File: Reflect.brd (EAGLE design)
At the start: 36.6 x 9.1 mm, 8 parts

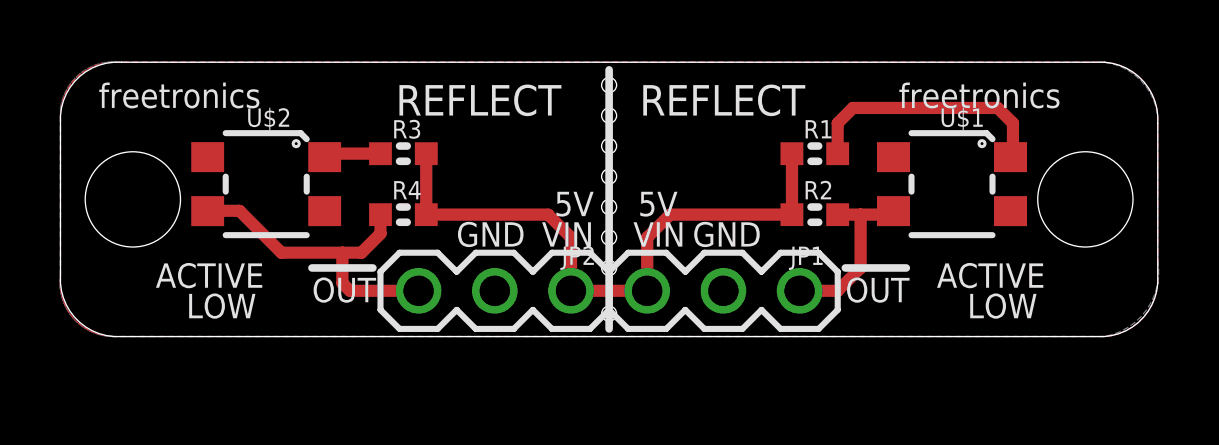
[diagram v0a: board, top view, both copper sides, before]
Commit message: Split ground pour into two halves to fix unrouted ground airwire. Added schematic note that although only one VCC pin needs to be connected both ground pins need to be connected if both sensors are used on an unsplit board.
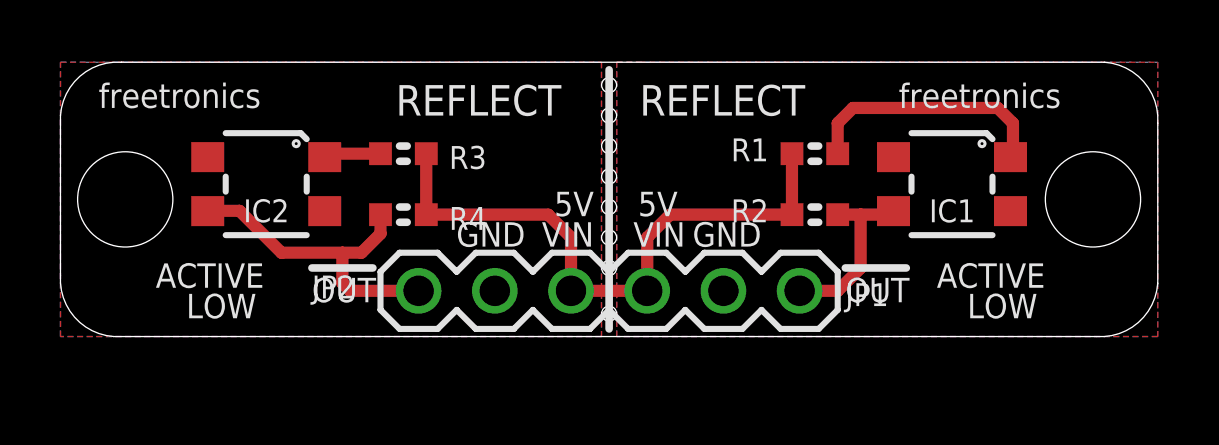
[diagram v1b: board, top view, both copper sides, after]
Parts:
- renumbered U$1 to IC1, U$2 to IC2
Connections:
- removed net GND: IC1.2, IC1.4, IC2.2, IC2.4, JP1.2, JP2.2
- new net GND1: IC2.2, IC2.4, JP2.2
- new net GND2: IC1.2, IC1.4, JP1.2
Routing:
- added copper zone on layer 1, net GND1
- added copper zone on layer 16, net GND1
- added copper zone on layer 1, net GND2
- added copper zone on layer 16, net GND2
- removed copper zone on layer 1, net GND
- removed copper zone on layer 16, net GND

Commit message: New version with GNDs connected.
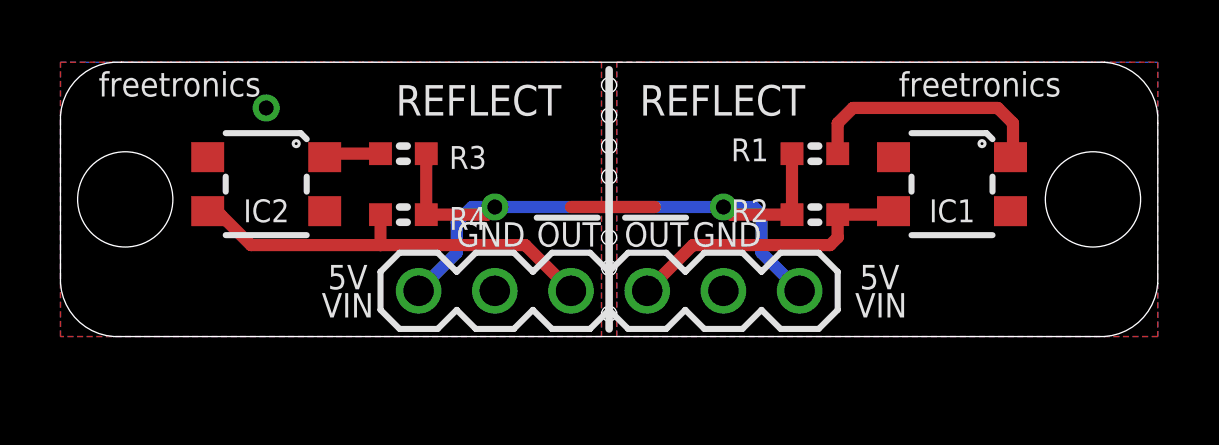
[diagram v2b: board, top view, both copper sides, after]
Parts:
- moved JP1 5.08 mm to (19.6, 1.52), flipped to the bottom
- moved JP2 5.08 mm to (11.9, 1.52), flipped to the bottom
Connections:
- removed net GND1: IC2.2, IC2.4, JP2.2
- removed net GND2: IC1.2, IC1.4, JP1.2
- new net GND: IC1.2, IC1.4, IC2.2, IC2.4, JP1.2, JP2.2
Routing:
- net VCC: track 20.4 -> 25.2 mm, vias 0 -> 2
- net OUT2: track 6.03 -> 9.76 mm
- net OUT1: track 10.9 -> 14.2 mm
- net GND: track 0.00 -> 2.79 mm, vias 0 -> 1
- added copper zone on layer 1, net GND
- added copper zone on layer 16, net GND
- removed copper zone on layer 1, net GND1
- removed copper zone on layer 16, net GND1
- removed copper zone on layer 1, net GND2
- removed copper zone on layer 16, net GND2
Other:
- board text added: "(5V)"
- board text removed: "ACTIVE"
- board text removed: "LOW"

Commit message: Tweaks to schematic and PCB for v1.0 release
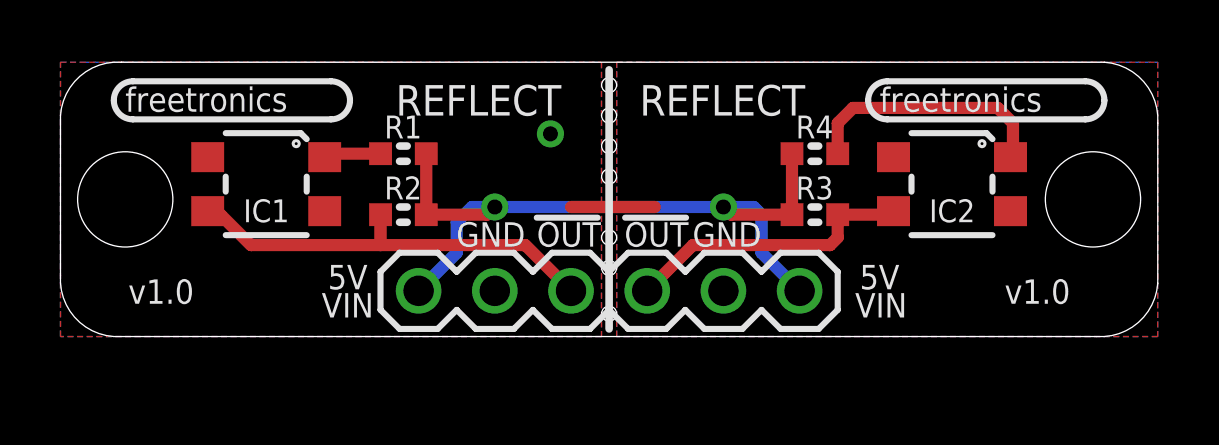
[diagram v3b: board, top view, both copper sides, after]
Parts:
- R1: value 100 -> 100R
- R3: value 100 -> 10k
- R4: value 10k -> 100R
- moved IC1 22.9 mm to (6.86, 5.08)
- moved IC2 22.9 mm to (29.7, 5.08)
- moved R3 13.9 mm to (25.1, 4.06)
- moved R4 13.9 mm to (25.1, 6.10)
- moved R1 13.7 mm to (11.4, 6.10)
- moved R2 13.7 mm to (11.4, 4.06)
- moved JP1 7.62 mm to (11.9, 1.52)
- moved JP2 7.62 mm to (19.6, 1.52)
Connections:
- net N$1: now also IC1.1, R1.1; no longer IC2.1, R3.1
- net N$3: now also IC2.1, R4.2; no longer IC1.1, R1.2
- net OUT1: now also IC1.3, JP1.3, R2.1; no longer IC2.3, JP2.3, R4.1
- net OUT2: now also IC2.3, JP2.1, R3.2; no longer IC1.3, JP1.1, R2.2
- net VCC: now also JP1.1, JP2.3, R1.2, R2.2, R3.1, R4.1; no longer JP1.3, JP2.1, R1.1, R2.1, R3.2, R4.2
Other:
- board text added: "v1.0"
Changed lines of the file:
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@@
 <?xml version="1.0" encoding="utf-8"?>
 <!DOCTYPE eagle SYSTEM "eagle.dtd">
-<eagle version="6.5.0">
+<eagle version="6.3">
 <drawing>
 <settings>
@@
 <setting verticaltext="up"/>
 </settings>
-<grid distance="0.005" unitdist="inch" unit="inch" style="dots" multiple="1" display="yes" altdistance="0.005" altunitdist="inch" altunit="inch"/>
+<grid distance="0.005" unitdist="inch" unit="inch" style="dots" multiple="1" display="no" altdistance="0.005" altunitdist="inch" altunit="inch"/>
 <layers>
 <layer number="1" name="Top" color="4" fill="1" visible="yes" active="yes"/>
@@
 <text x="11.176" y="7.366" size="1.016" layer="21" ratio="15">REFLECT</text>
 <text x="19.304" y="7.366" size="1.016" layer="21" ratio="15">REFLECT</text>
-<text x="27.94" y="8.001" size="0.8128" layer="21" ratio="15">freetronics</text>
-<text x="1.27" y="8.001" size="0.8128" layer="21" ratio="15">freetronics</text>
+<text x="2.159" y="7.493" size="0.8128" layer="21" ratio="15">freetronics</text>
 <text x="12.954" y="3.048" size="0.8128" layer="22" font="vector" ratio="15" rot="MR0">VIN</text>
 <text x="23.114" y="3.048" size="0.8128" layer="22" font="vector" ratio="15" rot="MR0">GND</text>
@@
 <wire x1="23.368" y1="2.159" x2="24.003" y2="2.794" width="0.2032" layer="21"/>
 <text x="28.2194" y="1.4478" size="0.8128" layer="21" font="vector" ratio="15" rot="R180">VIN</text>
+<text x="2.2606" y="1.0922" size="0.8128" layer="21" font="vector" ratio="15">v1.0</text>
+<text x="31.4706" y="1.0922" size="0.8128" layer="21" font="vector" ratio="15">v1.0</text>
+<wire x1="2.413" y1="8.509" x2="1.778" y2="7.874" width="0.2032" layer="21" curve="90"/>
+<wire x1="1.778" y1="7.874" x2="2.413" y2="7.239" width="0.2032" layer="21" curve="90"/>
+<wire x1="2.413" y1="7.239" x2="9.017" y2="7.239" width="0.2032" layer="21"/>
+<wire x1="9.017" y1="7.239" x2="9.652" y2="7.874" width="0.2032" layer="21" curve="90"/>
+<wire x1="9.652" y1="7.874" x2="9.017" y2="8.509" width="0.2032" layer="21" curve="90"/>
+<wire x1="9.017" y1="8.509" x2="2.413" y2="8.509" width="0.2032" layer="21"/>
+<text x="27.305" y="7.493" size="0.8128" layer="21" ratio="15">freetronics</text>
+<wire x1="27.559" y1="8.509" x2="26.924" y2="7.874" width="0.2032" layer="21" curve="90"/>
+<wire x1="26.924" y1="7.874" x2="27.559" y2="7.239" width="0.2032" layer="21" curve="90"/>
+<wire x1="27.559" y1="7.239" x2="34.163" y2="7.239" width="0.2032" layer="21"/>
+<wire x1="34.163" y1="7.239" x2="34.798" y2="7.874" width="0.2032" layer="21" curve="90"/>
+<wire x1="34.798" y1="7.874" x2="34.163" y2="8.509" width="0.2032" layer="21" curve="90"/>
+<wire x1="34.163" y1="8.509" x2="27.559" y2="8.509" width="0.2032" layer="21"/>
+<circle x="7.874" y="6.477" radius="0.127" width="0.2032" layer="51"/>
+<circle x="30.734" y="6.477" radius="0.127" width="0.2032" layer="51"/>
 </plain>
 <attributes>
@@
 </autorouter>
 <elements>
-<element name="IC1" library="freetronics-original" package="QRE1113GR" value="QRE1113GR" x="29.718" y="5.08" smashed="yes" rot="R180">
+<element name="IC2" library="freetronics-original" package="QRE1113GR" value="QRE1113GR" x="29.718" y="5.08" smashed="yes" rot="R180">
 <attribute name="NAME" x="28.956" y="3.81" size="0.762" layer="25" ratio="15"/>
 <attribute name="VALUE" x="26.416" y="7.112" size="0.762" layer="27" ratio="15"/>
 </element>
-<element name="R1" library="freetronics-original" package="0603" value="100" x="25.146" y="6.096" smashed="yes">
-<attribute name="NAME" x="22.352" y="5.842" size="0.762" layer="25" font="vector" ratio="15"/>
+<element name="R4" library="freetronics-original" package="0603" value="100R" x="25.146" y="6.096" smashed="yes">
+<attribute name="NAME" x="24.511" y="6.604" size="0.762" layer="25" font="vector" ratio="15"/>
 <attribute name="VALUE" x="24.384" y="5.588" size="0.762" layer="27" font="vector" ratio="15"/>
 </element>
-<element name="R2" library="freetronics-original" package="0603" value="10k" x="25.146" y="4.064" smashed="yes">
-<attribute name="NAME" x="22.352" y="3.81" size="0.762" layer="25" font="vector" ratio="15"/>
+<element name="R3" library="freetronics-original" package="0603" value="10k" x="25.146" y="4.064" smashed="yes">
+<attribute name="NAME" x="24.511" y="4.572" size="0.762" layer="25" font="vector" ratio="15"/>
 <attribute name="VALUE" x="24.384" y="3.81" size="0.762" layer="27" font="vector" ratio="15"/>
 </element>
-<element name="JP1" library="freetronics-original" package="1X03" value="" x="19.558" y="1.524" smashed="yes" rot="MR180">
+<element name="JP2" library="freetronics-original" package="1X03" value="" x="19.558" y="1.524" smashed="yes" rot="MR180">
 <attribute name="NAME" x="18.034" y="1.016" size="0.762" layer="26" ratio="15" rot="MR0"/>
 <attribute name="VALUE" x="18.288" y="4.699" size="1.27" layer="28" rot="MR180"/>
 </element>
-<element name="IC2" library="freetronics-original" package="QRE1113GR" value="QRE1113GR" x="6.858" y="5.08" smashed="yes" rot="R180">
+<element name="IC1" library="freetronics-original" package="QRE1113GR" value="QRE1113GR" x="6.858" y="5.08" smashed="yes" rot="R180">
 <attribute name="NAME" x="6.096" y="3.81" size="0.762" layer="25" ratio="15"/>
 <attribute name="VALUE" x="3.81" y="7.112" size="0.762" layer="27" ratio="15"/>
 </element>
-<element name="R3" library="freetronics-original" package="0603" value="100" x="11.43" y="6.096" smashed="yes">
-<attribute name="NAME" x="12.954" y="5.588" size="0.762" layer="25" font="vector" ratio="15"/>
+<element name="R1" library="freetronics-original" package="0603" value="100R" x="11.43" y="6.096" smashed="yes">
+<attribute name="NAME" x="10.795" y="6.604" size="0.762" layer="25" font="vector" ratio="15"/>
 <attribute name="VALUE" x="10.668" y="5.842" size="0.762" layer="27" font="vector" ratio="15"/>
 </element>
-<element name="R4" library="freetronics-original" package="0603" value="10k" x="11.43" y="4.064" smashed="yes">
-<attribute name="NAME" x="12.954" y="3.556" size="0.762" layer="25" font="vector" ratio="15"/>
+<element name="R2" library="freetronics-original" package="0603" value="10k" x="11.43" y="4.064" smashed="yes">
+<attribute name="NAME" x="10.795" y="4.572" size="0.762" layer="25" font="vector" ratio="15"/>
 <attribute name="VALUE" x="10.668" y="3.81" size="0.762" layer="27" font="vector" ratio="15"/>
 </element>
-<element name="JP2" library="freetronics-original" package="1X03" value="" x="11.938" y="1.524" smashed="yes" rot="MR180">
+<element name="JP1" library="freetronics-original" package="1X03" value="" x="11.938" y="1.524" smashed="yes" rot="MR180">
 <attribute name="NAME" x="20.574" y="1.27" size="0.762" layer="26" ratio="15" rot="MR0"/>
 <attribute name="VALUE" x="10.668" y="4.699" size="1.27" layer="28" rot="MR180"/>
@@
 <signals>
 <signal name="OUT2">
-<contactref element="JP1" pad="1"/>
-<contactref element="R2" pad="2"/>
-<contactref element="IC1" pad="3"/>
+<contactref element="JP2" pad="1"/>
+<contactref element="R3" pad="2"/>
+<contactref element="IC2" pad="3"/>
 <wire x1="25.908" y1="4.064" x2="27.652" y2="4.064" width="0.4064" layer="1"/>
 <wire x1="27.652" y1="4.064" x2="27.768" y2="4.18" width="0.4064" layer="1"/>
@@
 </signal>
 <signal name="VCC">
-<contactref element="JP1" pad="3"/>
-<contactref element="JP2" pad="1"/>
-<contactref element="R4" pad="2"/>
-<contactref element="R3" pad="2"/>
+<contactref element="JP2" pad="3"/>
+<contactref element="JP1" pad="1"/>
+<contactref element="R2" pad="2"/>
+<contactref element="R1" pad="2"/>
 <wire x1="12.192" y1="4.064" x2="12.192" y2="6.096" width="0.4064" layer="1"/>
-<contactref element="R1" pad="1"/>
-<contactref element="R2" pad="1"/>
+<contactref element="R4" pad="1"/>
+<contactref element="R3" pad="1"/>
 <wire x1="24.384" y1="4.064" x2="24.384" y2="6.096" width="0.4064" layer="1"/>
 <wire x1="12.192" y1="4.064" x2="14.224" y2="4.064" width="0.4064" layer="1"/>
@@
 </signal>
 <signal name="N$1">
-<contactref element="R3" pad="1"/>
-<contactref element="IC2" pad="1"/>
+<contactref element="R1" pad="1"/>
+<contactref element="IC1" pad="1"/>
 <wire x1="8.819" y1="5.969" x2="8.808" y2="5.98" width="0.4064" layer="1"/>
 <wire x1="10.668" y1="6.096" x2="8.924" y2="6.096" width="0.4064" layer="1"/>
@@
 </signal>
 <signal name="OUT1">
-<contactref element="JP2" pad="3"/>
-<contactref element="R4" pad="1"/>
-<contactref element="IC2" pad="3"/>
+<contactref element="JP1" pad="3"/>
+<contactref element="R2" pad="1"/>
+<contactref element="IC1" pad="3"/>
 <wire x1="5.08" y1="4.064" x2="5.334" y2="4.064" width="0.4064" layer="1"/>
 <wire x1="5.334" y1="4.064" x2="6.35" y2="3.048" width="0.4064" layer="1"/>
@@
 </signal>
 <signal name="N$3">
-<contactref element="IC1" pad="1"/>
-<contactref element="R1" pad="2"/>
+<contactref element="IC2" pad="1"/>
+<contactref element="R4" pad="2"/>
 <wire x1="31.668" y1="5.98" x2="31.75" y2="5.98" width="0.4064" layer="1"/>
 <wire x1="31.75" y1="5.98" x2="31.75" y2="7.112" width="0.4064" layer="1"/>
@@
 </signal>
 <signal name="GND">
+<contactref element="JP1" pad="2"/>
 <contactref element="JP2" pad="2"/>
-<contactref element="JP1" pad="2"/>
-<contactref element="IC1" pad="4"/>
-<contactref element="IC1" pad="2"/>
+<contactref element="IC2" pad="4"/>
+<contactref element="IC2" pad="2"/>
 <polygon width="0.2032" layer="1">
 <vertex x="19.304" y="9.144"/>
@@
 <vertex x="18.542" y="0"/>
 </polygon>
-<contactref element="IC2" pad="2"/>
-<contactref element="IC2" pad="4"/>
+<contactref element="IC1" pad="2"/>
+<contactref element="IC1" pad="4"/>
 <polygon width="0.2032" layer="1">
 <vertex x="0" y="9.144"/>
@@
 </polygon>
 <wire x1="19.812" y1="4.318" x2="17.018" y2="4.318" width="0.4064" layer="1"/>
-<via x="6.858" y="7.62" extent="1-16" drill="0.5"/>
+<via x="16.3322" y="6.7564" extent="1-16" drill="0.5"/>
 </signal>
 </signals>
+<errors>
+</errors>
 </board>
 </drawing>

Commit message: Changes for v1.0 release: moved headers; changed track size; changed overllay
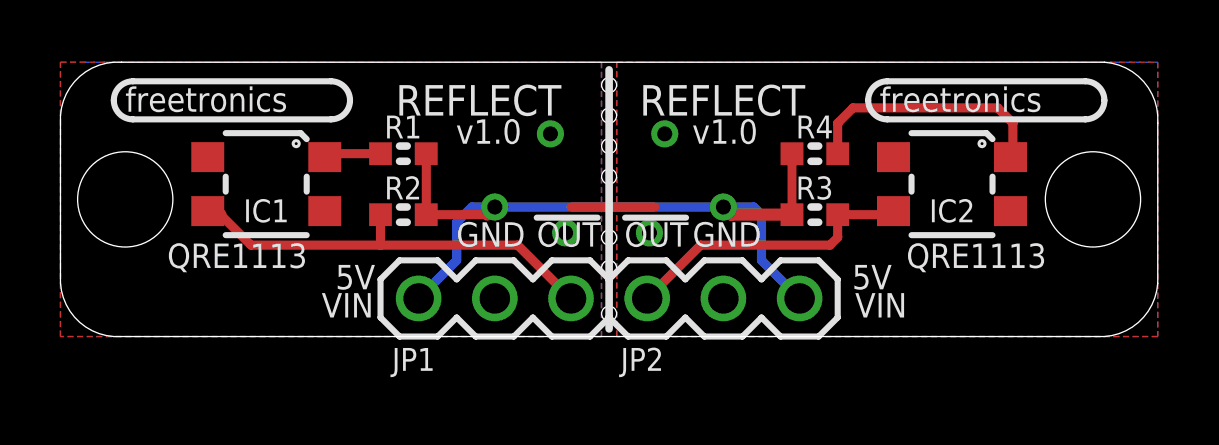
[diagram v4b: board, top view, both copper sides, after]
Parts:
- moved JP1 0.25 mm to (11.9, 1.27)
- moved JP2 0.25 mm to (19.6, 1.27)
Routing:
- net VCC: track 25.2 -> 25.7 mm
- net GND: vias 1 -> 4
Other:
- board text added: "QRE1113"
- board text added: "freetronics.com/reflect"
- board text removed: "(5V)"
- board text removed: "www.freetronics.com/reflect"
